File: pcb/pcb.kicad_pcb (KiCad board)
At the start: 4 copper layers, 281 parts, among them J100 Conn_02x05_Odd_Even, J101 Conn_02x05_Odd_Even, J102 Conn_02x05_Odd_Even, J400 AudioJack4, J500 FPC_18P_1.0MM, J600 USB_B_Micro, J601 USB_A, Q300 IRLML6402, Q302 2SK3018, Q500 IRLML6402, Q800 IRLML6402, SW700 SW_Push, SW701 SW_Push, SW702 SW_Push, SW703 SW_Push, SW704 SW_Push, SW705 SW_Push, SW706 SW_Push, SW707 SW_Push, U1 LTC3456, U100 MCIMX7S5EVM08SC, U2 LTC3549, U200 IS43LD16128B, U3 LTC3549, U300 ADP123, U301 W25Q16BV, U400 CS43130, U401 ADP150-3.0, U402 ADP150-1.8, U403 ADP150-1.8, U500 XC2C32A, U501 ADP5075, U502 LM324, U600 USBLC6-2SC6, U800 RTL8723BS, X400 DSC1001CE2-022.5792, Y100 24MHz, Y101 32.768kHz

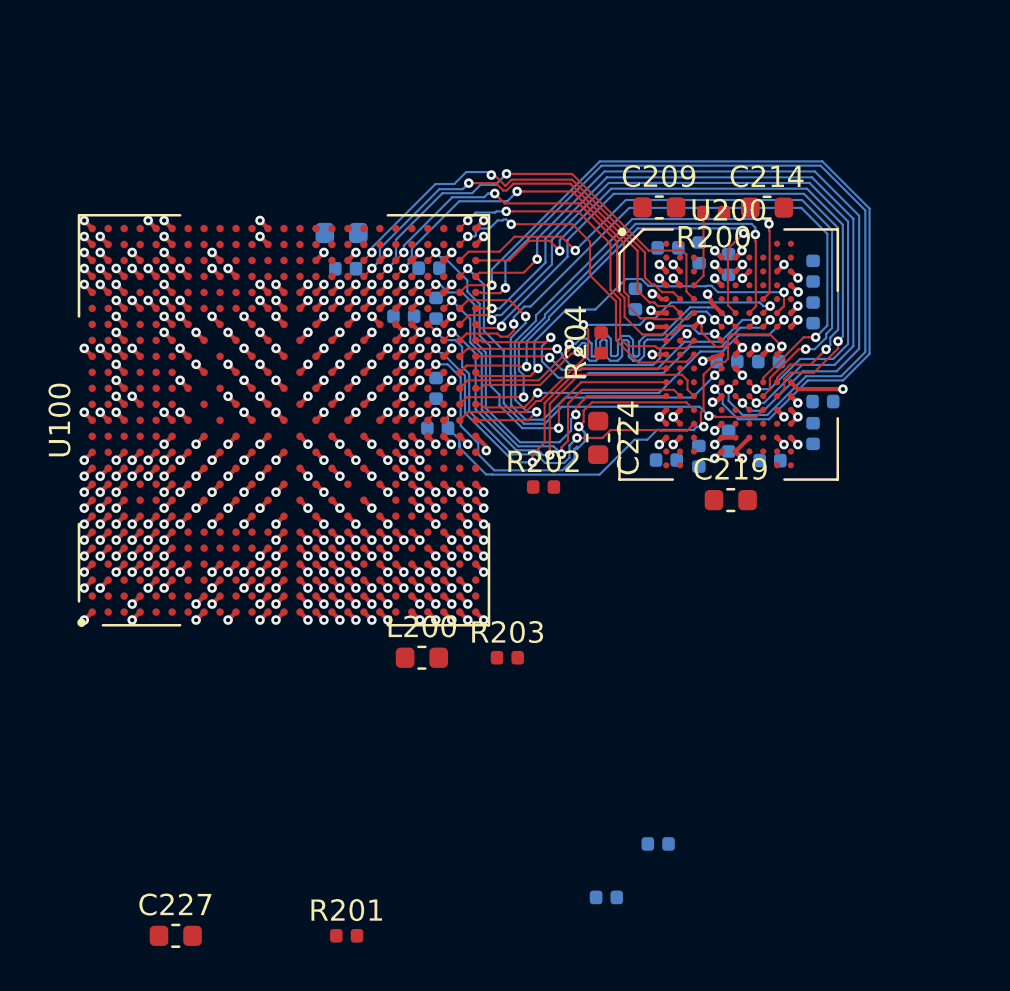
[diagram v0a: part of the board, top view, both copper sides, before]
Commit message: pcb: layout lpddr2
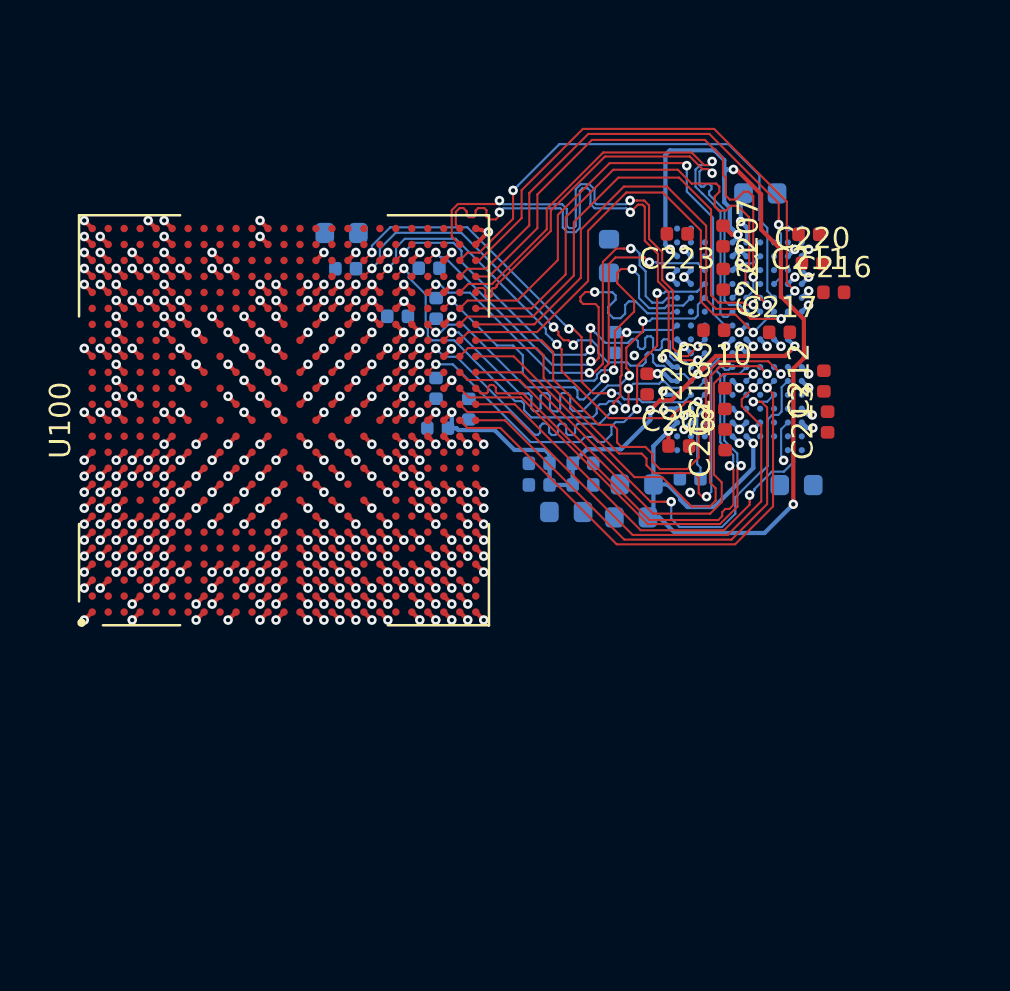
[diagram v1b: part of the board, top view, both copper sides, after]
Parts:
- C207, C208, C210, C211, C212, C213, C215, C216, C217, C218, C220, C221, C222, C223: moved to F.Cu
- C209, C214, C219, C224, C227, L200, R200, R201, R202, R203, R204, U200: moved to B.Cu
- moved C227 27.0 mm to (86.6, 123.4), turned to 180 degrees
- moved R201 25.4 mm to (82.0, 118.6), turned to 90 degrees
- moved C225 19.4 mm to (87.4, 122.2), turned to 180 degrees
- moved C226 17.8 mm to (85.3, 122.2), turned to 180 degrees
- moved C219 14.5 mm to (95.7, 108.5)
- moved C214 13.1 mm to (97.4, 122.2)
- moved C209 13.0 mm to (89.9, 122.2), turned to 180 degrees
- moved R200 12.5 mm to (92.4, 121.9), turned to 0 degrees
- moved L200 11.8 mm to (89.7, 123.7)
- moved C223 10.6 mm to (91.8, 110.4)
- moved C207 10.4 mm to (94.0, 110.5), turned to 270 degrees
- moved C220 9.47 mm to (98.2, 111.8)
- moved C211 9.35 mm to (98.0, 110.4), turned to 180 degrees
- moved C208 9.31 mm to (91.9, 120.3)
- moved R203 9.25 mm to (85.3, 121.2), turned to 180 degrees
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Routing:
- net +DRAM_1V8: track 3.67 -> 55.4 mm, vias 4 -> 6
- net /ddr/DRAM_SDQSN_0: track 39.7 -> 24.4 mm, vias 2 -> 1
- net /ddr/DRAM_SDQSP_0: track 37.8 -> 24.4 mm, vias 2 -> 1
- net /ddr/DRAM_DATA4: track 35.0 -> 23.9 mm, vias 2 -> 1
- net /ddr/DRAM_DATA5: track 34.0 -> 23.4 mm, vias 2 -> 1
- net /ddr/DRAM_DATA2: track 33.9 -> 24.1 mm, vias 2 -> 1
- net /ddr/DRAM_DQM1: track 14.7 -> 23.3 mm, vias 2 -> 1
- net /ddr/DRAM_DATA10: track 15.3 -> 23.7 mm, vias 2 -> 1
- net GND: track 103.2 -> 95.2 mm, vias 174 -> 172
- net /ddr/DRAM_CKN: track 16.5 -> 24.1 mm, vias 2 -> 3
- net /ddr/DRAM_CKP: track 16.5 -> 24.1 mm, vias 2 -> 3
- net /ddr/DRAM_DATA7: track 29.9 -> 23.4 mm, vias 2 -> 1
- net /ddr/DRAM_DATA8: track 17.2 -> 23.6 mm, vias 2 -> 1
- net /ddr/DRAM_DATA3: track 30.0 -> 24.1 mm, vias 2 -> 1
- net /ddr/DRAM_DATA1: track 29.3 -> 23.7 mm, vias 2 -> 1
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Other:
- net class DDR removed
- net class DDR_CTRL added: clearance 0.0895, trace_width 0.1, via_dia 0.45, via_drill 0.2
- net class DDR_DQH added: clearance 0.0895, trace_width 0.1, via_dia 0.45, via_drill 0.2
- net class DDR_DQL added: clearance 0.0895, trace_width 0.1, via_dia 0.45, via_drill 0.2
- net class POWER_8MIL added: clearance 0.1, trace_width 0.2, via_dia 0.45, via_drill 0.2

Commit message: pcb: working on layout
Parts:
- removed C701: 220nF, Capacitor_SMD:C_0402_1005Metric
- removed R100: 100K, Resistor_SMD:R_0603_1608Metric
- removed R101: 0, Resistor_SMD:R_0603_1608Metric
- added D3: LED, LED_THT:LED_D5.0mm, B.Cu at (180.1, 58.8)
- added R13: 1K, Resistor_SMD:R_0603_1608Metric, F.Cu at (71.2, 1.94)
- added SW1: SW_SPDT, Button_Switch_SMD:SW_SPDT_PCM12, F.Cu at (174.2, 46.4)
- BT_Backup1: footprint Battery:BatteryHolder_Keystone_1060_1x2032 -> footprints:BatteryHolder_CR1220; moved to B.Cu
- C15, C16, C17, C18, C19, C20, C21, C22, C23, C24, C25, C26, C27, C28, C29, C30, C305, C306, C307, C308, C309, C31, C313, C33, C34, C35, C36, C37, C38, C40, C41, C504, C505, C506, C507, C601, C602, C603, C604, C605, C606, C700, C702, C703, L700, SW700, SW701, SW702, SW703, SW704, SW705, SW706, SW707: moved to B.Cu
- C600: footprint Capacitor_SMD:C_0805_2012Metric -> Capacitor_SMD:C_0603_1608Metric
- L1, L2, L3, L4, L5, L500: footprint Inductor_SMD:L_Vishay_IHLP-4040 -> Inductor_SMD:L_Vishay_IHLP-1212
- L6: footprint Inductor_SMD:L_0603_1608Metric -> Inductor_SMD:L_0402_1005Metric; moved to B.Cu
- R601, R602, R603, R605, R606, R607: footprint Resistor_SMD:R_0805_2012Metric -> Resistor_SMD:R_0603_1608Metric; moved to B.Cu
- R604, R608: footprint Resistor_SMD:R_0805_2012Metric -> Resistor_SMD:R_0603_1608Metric
- U500: value XC2C32A -> XC2C32A_QF32; footprint Package_QFP:LQFP-44_10x10mm_P0.8mm -> Package_DFN_QFN:QFN-32-1EP_5x5mm_P0.5mm_EP3.1x3.1mm
- U502: footprint Package_SO:SOIC-16_3.9x9.9mm_P1.27mm -> Package_SO:TSSOP-14_4.4x5mm_P0.65mm
- moved BT_Backup1 217.9 mm to (173.2, 148.4)
- moved BT1 197.5 mm to (127.2, 118.4)
- moved D1 190.5 mm to (164.1, 144.8)
- moved R400 161.0 mm to (160.5, 151.7)
- moved U403 159.3 mm to (152.2, 156.6)
- moved J400 159.1 mm to (144.9, 151.9), turned to 90 degrees
- moved U400 156.8 mm to (153.9, 149.7), turned to 270 degrees
- moved U401 155.9 mm to (159.1, 154.7), turned to 90 degrees
- moved L400 155.2 mm to (163.6, 148.7), turned to 270 degrees
- moved C416 154.4 mm to (151.4, 153.8), turned to 270 degrees
- moved C414 154.3 mm to (150.2, 152.1), turned to 90 degrees
- moved X400 153.9 mm to (159.8, 149.2), turned to 180 degrees
- moved L401 152.8 mm to (158.0, 146.2), turned to 180 degrees
- moved R404 152.6 mm to (154.8, 156.3), turned to 90 degrees
- moved C405 151.6 mm to (159.5, 157.2), turned to 180 degrees
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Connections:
- net /ddr/DRAM_CKE renamed Net-(R204-Pad1)
- net /ddr/DRAM_CKN renamed Net-(U100-PadAD25)
- net /ddr/DRAM_CKP renamed Net-(U100-PadAD24)
- net /ddr/DRAM_CS renamed Net-(U100-PadAB23)
- RN100 pad 6: BT_CFG_11 -> BT_CFG_14
- RN100 pad 8: BT_CFG_14 -> BT_CFG_11
- RN101 pad 7: BT_CFG_5 -> BT_CFG_6
- RN101 pad 8: BT_CFG_6 -> BT_CFG_5
- RN501 pad 5: Net-(RN501-Pad5) -> (no net)
- RN501 pad 6: Net-(RN501-Pad6) -> (no net)
- RN502 pad 5: /lcd/LCD_D0 -> /lcd/LCD_D1
- RN502 pad 6: /lcd/LCD_ST -> /lcd/LCD_CP
- RN502 pad 7: /lcd/LCD_CPL -> /lcd/LCD_FR
- RN502 pad 8: /lcd/LCD_CPG -> /lcd/LCD_S
- RN503 pad 5: /lcd/LCD_S -> /lcd/LCD_CPG
- RN503 pad 6: /lcd/LCD_FR -> /lcd/LCD_CPL
- RN503 pad 7: /lcd/LCD_CP -> /lcd/LCD_ST
- RN503 pad 8: /lcd/LCD_D1 -> /lcd/LCD_D0
- SW700 pad 1: /keypad/SW_SE -> SW_SE
- SW701 pad 1: /keypad/SW_ST -> SW_ST
- SW702 pad 1: /keypad/SW_A -> SW_A
- SW703 pad 1: /keypad/SW_B -> SW_B
- SW704 pad 1: /keypad/SW_UP -> SW_UP
- SW705 pad 1: /keypad/SW_LE -> SW_LE
- SW706 pad 1: /keypad/SW_RI -> SW_RI
- SW707 pad 1: /keypad/SW_DN -> SW_DN
- U1 pad 18: USB_SUSPEND -> (no net)
- U1 pad 19: (no net) -> /power/PWR_KEY
- U100 pad AA4: USB_SUSPEND -> (no net)
- U100 pad G24: (no net) -> SW_ST
- U100 pad G25: (no net) -> SW_SE
- U100 pad H24: (no net) -> SW_A
- U100 pad H25: (no net) -> SW_B
- U100 pad J24: (no net) -> SW_LE
- U100 pad J25: (no net) -> SW_UP
- U100 pad K24: (no net) -> SW_RI
- U100 pad K25: (no net) -> SW_DN
- U100 pad N1: /keypad/SW_SE -> (no net)
- U100 pad N2: /keypad/SW_ST -> (no net)
- U100 pad N3: /keypad/SW_A -> (no net)
- U100 pad N5: /keypad/SW_B -> (no net)
- U100 pad N6: /keypad/SW_UP -> (no net)
- U100 pad P1: /keypad/SW_LE -> (no net)
- U100 pad P2: /keypad/SW_RI -> (no net)
- U100 pad P3: /keypad/SW_DN -> (no net)
- U100 pad P6: Net-(R100-Pad1) -> GND
- U100 pad W3: Net-(R101-Pad2) -> GND
- U100 pad Y4: EXT_PWR_GOOD -> (no net)
- U500 pad 1: Net-(RN503-Pad3) -> Net-(RN502-Pad3)
- U500 pad 10: CPLD_JTAG_TMS -> Net-(RN501-Pad7)
- U500 pad 11: CPLD_JTAG_TCK -> GND
- U500 pad 12: (no net) -> +3V3
- U500 pad 14: (no net) -> CPLD_JTAG_TDI
- U500 pad 15: +1V8 -> CPLD_JTAG_TMS
- U500 pad 16: (no net) -> CPLD_JTAG_TCK
- U500 pad 17: GND -> (no net)
- U500 pad 2: Net-(RN503-Pad4) -> Net-(RN502-Pad2)
- U500 pad 20: (no net) -> +1V8
- U500 pad 21: (no net) -> GND
- U500 pad 24: CPLD_JTAG_TDO -> (no net)
- U500 pad 25: GND -> CPLD_JTAG_TDO
- U500 pad 26: +3V3 -> GND
- U500 pad 27: (no net) -> +1V8
- U500 pad 28: (no net) -> Net-(RN503-Pad4)
- U500 pad 29: (no net) -> Net-(RN503-Pad3)
- U500 pad 3: (no net) -> Net-(RN502-Pad1)
- U500 pad 30: Net-(RN501-Pad5) -> Net-(RN503-Pad2)
- U500 pad 31: Net-(RN501-Pad6) -> Net-(RN503-Pad1)
- U500 pad 32: Net-(RN501-Pad7) -> Net-(RN502-Pad4)
- U500 pad 33: Net-(RN501-Pad8) -> (no net)
- U500 pad 4: GND -> +3V3
- U500 pad 5: (no net) -> Net-(RN500-Pad8)
- U500 pad 6: (no net) -> Net-(RN500-Pad7)
- U500 pad 7: +1V8 -> Net-(RN500-Pad6)
- U500 pad 8: (no net) -> Net-(RN500-Pad5)
- U500 pad 9: CPLD_JTAG_TDI -> Net-(RN501-Pad8)
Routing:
- net Net-(D600-Pad1): track 0.53 -> 83.0 mm, vias 1 -> 2
- net Net-(R601-Pad1): track 0.53 -> 78.3 mm
- net Net-(R602-Pad1): track 0.53 -> 76.5 mm
- net SAI1_TXD: track 0.53 -> 62.9 mm
- net SAI1_MCLK: track 0.53 -> 62.0 mm
- net SAI1_TXC: track 0.53 -> 61.0 mm
- net SAI1_TXFS: track 0.53 -> 60.0 mm
- net SW_ST: track 0.00 -> 35.3 mm
- net SW_SE: track 0.00 -> 35.0 mm
- net SW_A: track 0.00 -> 34.2 mm
- net SW_B: track 0.00 -> 33.7 mm
- net SW_LE: track 0.00 -> 32.9 mm
- net Net-(R606-Pad1): track 0.53 -> 33.3 mm
- net SW_UP: track 0.00 -> 32.7 mm
- net SW_RI: track 0.00 -> 31.7 mm
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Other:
- net class Default: clearance 0.1 -> 0.0895
- net class POWER_8MIL: clearance 0.1 -> 0.0895
- rule trace_clearance: 0.1 -> 0.0895
- board text added: "RhythmPocket"
